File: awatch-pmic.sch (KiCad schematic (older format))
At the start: 16 parts, among them J301 Conn_01x02, U301 MAX14690

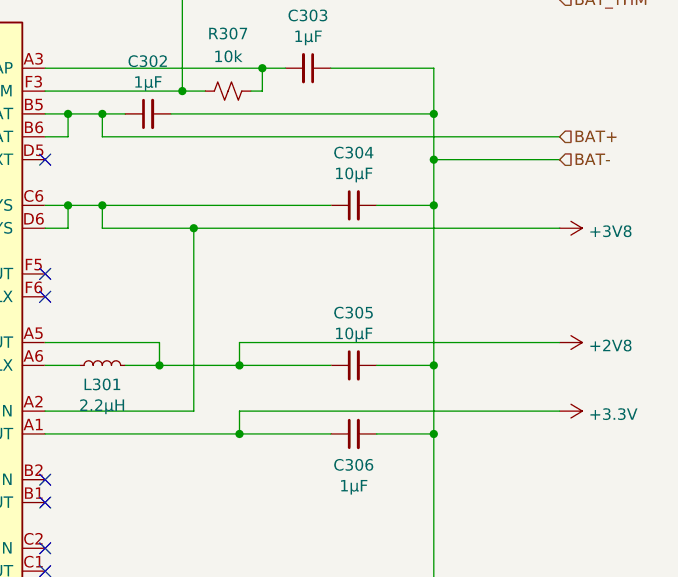
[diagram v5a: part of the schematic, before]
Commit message: Add footprints.
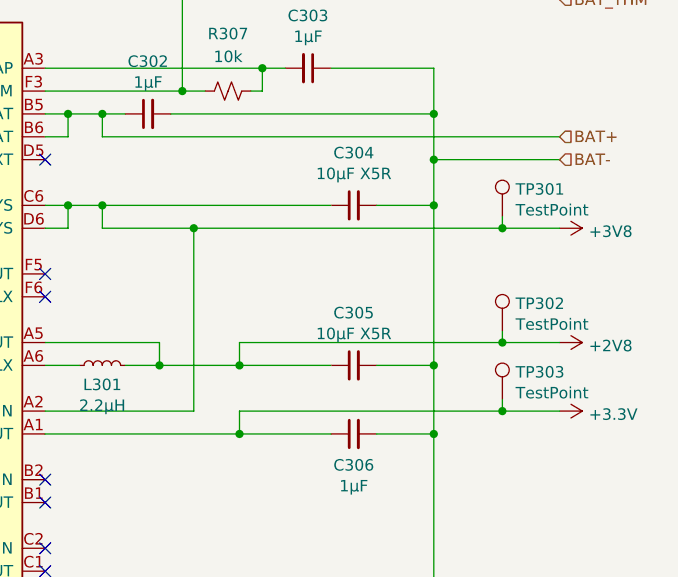
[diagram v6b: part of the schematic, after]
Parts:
- added TP301, TP302, TP303: TestPoint, TestPoint:TestPoint_Pad_D1.5mm, symbol Connector:TestPoint
- C301, C302, C303, C306: footprint (none) -> Capacitor_SMD:C_0603_1608Metric
- C304, C305: value 10µF -> 10µF X5R; footprint (none) -> Capacitor_SMD:C_0603_1608Metric
- J301: footprint (none) -> Connector_PinSocket_2.54mm:PinSocket_1x02_P2.54mm_Vertical
- L301: footprint (none) -> Inductor_SMD:L_0603_1608Metric
- R301, R302, R303, R304, R305, R306, R307: footprint (none) -> Resistor_SMD:R_0603_1608Metric
- U301: footprint (none) -> awatch2-footprints:WLP-36_2.69x2.44mm_Layout6x6_P0.4mm_Ball0.22mm_Pad0.2mm_NSMD
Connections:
- net +2V8: now also TP302.1
- net +3V3: now also TP303.1
- net +3V8: now also TP301.1
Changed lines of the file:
@@
 EESchema Schematic File Version 4
+LIBS:awatch2-cache
 EELAYER 26 0
 EELAYER END
@@
 F 0 "R302" H 3532 3554 50  0000 R CNN
 F 1 "10k" H 3532 3645 50  0000 R CNN
-F 2 "" H 3600 3600 50  0001 C CNN
+F 2 "Resistor_SMD:R_0603_1608Metric" H 3600 3600 50  0001 C CNN
 F 3 "~" H 3600 3600 50  0001 C CNN
 	1    3600 3600
@@
 F 0 "C301" H 3542 2096 50  0000 L CNN
 F 1 "1µF" H 3542 2005 50  0000 L CNN
-F 2 "" H 3450 2050 50  0001 C CNN
+F 2 "Capacitor_SMD:C_0603_1608Metric" H 3450 2050 50  0001 C CNN
 F 3 "~" H 3450 2050 50  0001 C CNN
 	1    3450 2050
@@
 F 0 "R304" V 3795 2200 50  0000 C CNN
 F 1 "12.5k" V 3886 2200 50  0000 C CNN
-F 2 "" H 4000 2200 50  0001 C CNN
+F 2 "Resistor_SMD:R_0603_1608Metric" H 4000 2200 50  0001 C CNN
 F 3 "~" H 4000 2200 50  0001 C CNN
 	1    4000 2200
@@
 F 0 "C303" V 6771 2200 50  0000 C CNN
 F 1 "1µF" V 6862 2200 50  0000 C CNN
-F 2 "" H 7000 2200 50  0001 C CNN
+F 2 "Capacitor_SMD:C_0603_1608Metric" H 7000 2200 50  0001 C CNN
 F 3 "~" H 7000 2200 50  0001 C CNN
 	1    7000 2200
@@
 F 0 "R307" V 6400 2300 50  0000 C CNN
 F 1 "10k" V 6500 2300 50  0000 C CNN
-F 2 "" H 6650 2300 50  0001 C CNN
+F 2 "Resistor_SMD:R_0603_1608Metric" H 6650 2300 50  0001 C CNN
 F 3 "~" H 6650 2300 50  0001 C CNN
 	1    6650 2300
@@
 F 0 "C302" V 6529 2400 50  0000 C CNN
 F 1 "1µF" V 6438 2400 50  0000 C CNN
-F 2 "" H 6300 2400 50  0001 C CNN
+F 2 "Capacitor_SMD:C_0603_1608Metric" H 6300 2400 50  0001 C CNN
 F 3 "~" H 6300 2400 50  0001 C CNN
 	1    6300 2400
@@
 P 7200 2800
 F 0 "C304" V 7429 2800 50  0000 C CNN
-F 1 "10µF" V 7338 2800 50  0000 C CNN
-F 2 "" H 7200 2800 50  0001 C CNN
+F 1 "10µF X5R" V 7338 2800 50  0000 C CNN
+F 2 "Capacitor_SMD:C_0603_1608Metric" H 7200 2800 50  0001 C CNN
 F 3 "~" H 7200 2800 50  0001 C CNN
 	1    7200 2800
@@
 F 0 "L301" V 6015 3500 50  0000 C CNN
 F 1 "2.2µH" V 5924 3500 50  0000 C CNN
-F 2 "" H 6100 3500 50  0001 C CNN
+F 2 "Inductor_SMD:L_0603_1608Metric" H 6100 3500 50  0001 C CNN
 F 3 "~" H 6100 3500 50  0001 C CNN
 	1    6100 3500
@@
 P 7200 3500
 F 0 "C305" V 7429 3500 50  0000 C CNN
-F 1 "10µF" V 7338 3500 50  0000 C CNN
-F 2 "" H 7200 3500 50  0001 C CNN
+F 1 "10µF X5R" V 7338 3500 50  0000 C CNN
+F 2 "Capacitor_SMD:C_0603_1608Metric" H 7200 3500 50  0001 C CNN
 F 3 "~" H 7200 3500 50  0001 C CNN
 	1    7200 3500
@@
 	6700 3500 6700 3400
 Wire Wire Line
-	6700 3400 8100 3400
+	6700 3400 7850 3400
 Connection ~ 6700 3500
 Wire Wire Line
@@
 F 0 "U301" H 5225 2166 50  0000 C CNN
 F 1 "MAX14690" H 5225 2075 50  0000 C CNN
-F 2 "" H 4700 2000 50  0001 C CNN
+F 2 "awatch2-footprints:WLP-36_2.69x2.44mm_Layout6x6_P0.4mm_Ball0.22mm_Pad0.2mm_NSMD" H 4700 2000 50  0001 C CNN
 F 3 "" H 4700 2000 50  0001 C CNN
 	1    4700 2000
@@
 F 0 "R306" V 3895 3800 50  0000 C CNN
 F 1 "0" V 3986 3800 50  0000 C CNN
-F 2 "" H 4100 3800 50  0001 C CNN
+F 2 "Resistor_SMD:R_0603_1608Metric" H 4100 3800 50  0001 C CNN
 F 3 "~" H 4100 3800 50  0001 C CNN
 	1    4100 3800
@@
 F 0 "R301" V 3650 2700 50  0000 C CNN
 F 1 "0" V 3750 2700 50  0000 C CNN
-F 2 "" H 3500 2700 50  0001 C CNN
+F 2 "Resistor_SMD:R_0603_1608Metric" H 3500 2700 50  0001 C CNN
 F 3 "~" H 3500 2700 50  0001 C CNN
 	1    3500 2700
@@
 F 0 "R303" V 3500 2800 50  0000 C CNN
 F 1 "0" V 3600 2800 50  0000 C CNN
-F 2 "" H 3750 2800 50  0001 C CNN
+F 2 "Resistor_SMD:R_0603_1608Metric" H 3750 2800 50  0001 C CNN
 F 3 "~" H 3750 2800 50  0001 C CNN
 	1    3750 2800
@@
 F 0 "R305" V 4113 3000 50  0000 C CNN
 F 1 "0" V 4204 3000 50  0000 C CNN
-F 2 "" H 4000 3000 50  0001 C CNN
+F 2 "Resistor_SMD:R_0603_1608Metric" H 4000 3000 50  0001 C CNN
 F 3 "~" H 4000 3000 50  0001 C CNN
 	1    4000 3000
@@
 F 0 "C306" V 7063 3800 50  0000 C CNN
 F 1 "1µF" V 6972 3800 50  0000 C CNN
-F 2 "" H 7200 3800 50  0001 C CNN
+F 2 "Capacitor_SMD:C_0603_1608Metric" H 7200 3800 50  0001 C CNN
 F 3 "~" H 7200 3800 50  0001 C CNN
 	1    7200 3800
@@
 	6700 3800 6700 3700
 Wire Wire Line
-	6700 3700 8100 3700
+	6700 3700 7850 3700
 Connection ~ 6700 3800
 Wire Wire Line
@@
 Connection ~ 6500 2900
 Wire Wire Line
-	6500 2900 8100 2900
+	6500 2900 7850 2900
 $Comp
 L power:+3.3V #PWR0134
@@
 F 0 "J301" H 3830 1542 50  0000 L CNN
 F 1 "Conn_01x02" H 3830 1451 50  0000 L CNN
-F 2 "" H 3750 1550 50  0001 C CNN
+F 2 "Connector_PinSocket_2.54mm:PinSocket_1x02_P2.54mm_Vertical" H 3750 1550 50  0001 C CNN
 F 3 "~" H 3750 1550 50  0001 C CNN
 	1    3750 1550
@@
 Wire Wire Line
 	6450 2300 6550 2300
+$Comp
+L Connector:TestPoint TP301
+U 1 1 5C869613
+P 7850 2850
+F 0 "TP301" H 7908 2970 50  0000 L CNN
+F 1 "TestPoint" H 7908 2879 50  0000 L CNN
+F 2 "TestPoint:TestPoint_Pad_D1.5mm" H 8050 2850 50  0001 C CNN
+F 3 "~" H 8050 2850 50  0001 C CNN
+	1    7850 2850
+	1    0    0    -1
+$EndComp
+Wire Wire Line
+	7850 2850 7850 2900
+Connection ~ 7850 2900
+Wire Wire Line
+	7850 2900 8100 2900
+$Comp
+L Connector:TestPoint TP302
+U 1 1 5C86C287
+P 7850 3350
+F 0 "TP302" H 7908 3470 50  0000 L CNN
+F 1 "TestPoint" H 7908 3379 50  0000 L CNN
+F 2 "TestPoint:TestPoint_Pad_D1.5mm" H 8050 3350 50  0001 C CNN
+F 3 "~" H 8050 3350 50  0001 C CNN
+	1    7850 3350
+	1    0    0    -1
+$EndComp
+Wire Wire Line
+	7850 3350 7850 3400
+Connection ~ 7850 3400
+Wire Wire Line
+	7850 3400 8100 3400
+$Comp
+L Connector:TestPoint TP303
+U 1 1 5C86F002
+P 7850 3650
+F 0 "TP303" H 7908 3770 50  0000 L CNN
+F 1 "TestPoint" H 7908 3679 50  0000 L CNN
+F 2 "TestPoint:TestPoint_Pad_D1.5mm" H 8050 3650 50  0001 C CNN
+F 3 "~" H 8050 3650 50  0001 C CNN
+	1    7850 3650
+	1    0    0    -1
+$EndComp
+Wire Wire Line
+	7850 3650 7850 3700
+Connection ~ 7850 3700
+Wire Wire Line
+	7850 3700 8100 3700
 $EndSCHEMATC

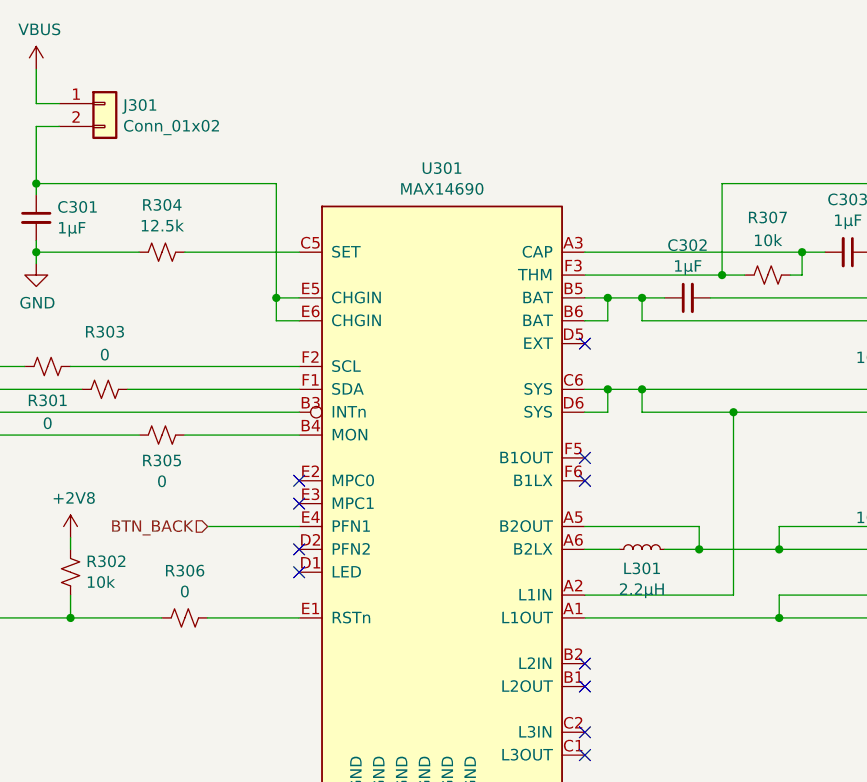
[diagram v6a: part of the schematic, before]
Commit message: PMIC relative placement and routing
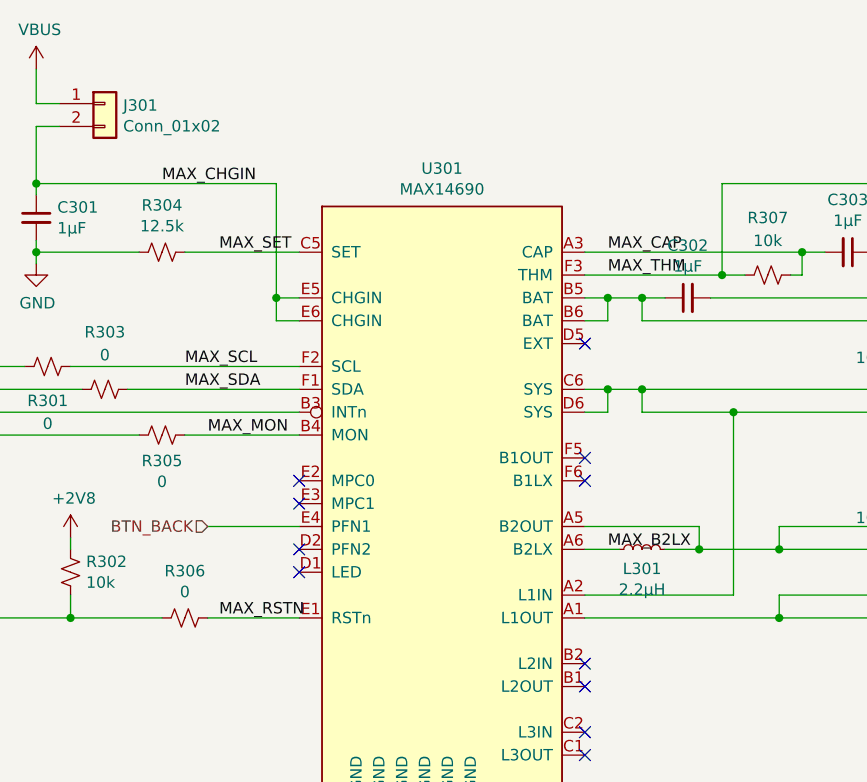
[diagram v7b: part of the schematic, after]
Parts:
- J301: footprint Connector_PinSocket_2.54mm:PinSocket_1x02_P2.54mm_Vertical -> Connector_PinHeader_2.54mm:PinHeader_1x02_P2.54mm_Vertical
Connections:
- net MAX_CAP: now reaches C303.2, R307.1, U301.A3 (CAP)
- net MAX_B2LX: now reaches L301.1, U301.A6 (B2LX)
- net MAX_MON: now reaches R305.1, U301.B4 (MON)
- net MAX_SET: now reaches R304.1, U301.C5 (SET)
- net MAX_RSTN: now reaches R306.1, U301.E1 (RSTn)
- net MAX_CHGIN: now reaches C301.1, J301.2 (Pin_2), U301.E5 (CHGIN), U301.E6 (CHGIN)
- net MAX_SDA: now reaches R303.1, U301.F1 (SDA)
- net MAX_SCL: now reaches R301.1, U301.F2 (SCL)
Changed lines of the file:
@@
 F 0 "J301" H 3830 1542 50  0000 L CNN
 F 1 "Conn_01x02" H 3830 1451 50  0000 L CNN
-F 2 "Connector_PinSocket_2.54mm:PinSocket_1x02_P2.54mm_Vertical" H 3750 1550 50  0001 C CNN
+F 2 "Connector_PinHeader_2.54mm:PinHeader_1x02_P2.54mm_Vertical" H 3750 1550 50  0001 C CNN
 F 3 "~" H 3750 1550 50  0001 C CNN
 	1    3750 1550
@@
 Wire Wire Line
 	7850 3700 8100 3700
+Text Label 4250 2200 0    50   ~ 0
+MAX_SET
+Text Label 4000 1900 0    50   ~ 0
+MAX_CHGIN
+Text Label 4100 2700 0    50   ~ 0
+MAX_SCL
+Text Label 4100 2800 0    50   ~ 0
+MAX_SDA
+Text Label 4200 3000 0    50   ~ 0
+MAX_MON
+Text Label 4250 3800 0    50   ~ 0
+MAX_RSTN
+Text Label 5950 2200 0    50   ~ 0
+MAX_CAP
+Text Label 5950 2300 0    50   ~ 0
+MAX_THM
+Text Label 5950 3500 0    50   ~ 0
+MAX_B2LX
 $EndSCHEMATC

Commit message: approx. final layout
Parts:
- C301, C302, C303, C306: value 1µF -> 1.0µF X7R; DigiKey PN (none) -> 1276-1946-1-ND
- C304, C305: DigiKey PN (none) -> 490-12538-1-ND
- U301: value MAX14690 -> MAX14690A; DigiKey PN (none) -> MOUSER: 700-MAX14690AEWX+
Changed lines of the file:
@@
 $Descr A4 11693 8268
 encoding utf-8
-Sheet 3 9
+Sheet 3 10
 Title "AWatch2"
 Date ""
@@
 P 3450 2050
 F 0 "C301" H 3542 2096 50  0000 L CNN
-F 1 "1µF" H 3542 2005 50  0000 L CNN
+F 1 "1.0µF X7R" H 3542 2005 50  0000 L CNN
 F 2 "Capacitor_SMD:C_0603_1608Metric" H 3450 2050 50  0001 C CNN
 F 3 "~" H 3450 2050 50  0001 C CNN
+F 4 "1276-1946-1-ND" H 0   0   50  0001 C CNN "DigiKey PN"
 	1    3450 2050
 	1    0    0    -1
@@
 P 7000 2200
 F 0 "C303" V 6771 2200 50  0000 C CNN
-F 1 "1µF" V 6862 2200 50  0000 C CNN
+F 1 "1.0µF X7R" V 6862 2200 50  0000 C CNN
 F 2 "Capacitor_SMD:C_0603_1608Metric" H 7000 2200 50  0001 C CNN
 F 3 "~" H 7000 2200 50  0001 C CNN
+F 4 "1276-1946-1-ND" H 0   0   50  0001 C CNN "DigiKey PN"
 	1    7000 2200
 	0    1    1    0
@@
 P 6300 2400
 F 0 "C302" V 6529 2400 50  0000 C CNN
-F 1 "1µF" V 6438 2400 50  0000 C CNN
+F 1 "1.0µF X7R" V 6438 2400 50  0000 C CNN
 F 2 "Capacitor_SMD:C_0603_1608Metric" H 6300 2400 50  0001 C CNN
 F 3 "~" H 6300 2400 50  0001 C CNN
+F 4 "1276-1946-1-ND" H 0   0   50  0001 C CNN "DigiKey PN"
 	1    6300 2400
 	0    -1   -1   0
@@
 F 2 "Capacitor_SMD:C_0603_1608Metric" H 7200 2800 50  0001 C CNN
 F 3 "~" H 7200 2800 50  0001 C CNN
+F 4 "490-12538-1-ND" H 0   0   50  0001 C CNN "DigiKey PN"
 	1    7200 2800
 	0    -1   -1   0
@@
 F 2 "Capacitor_SMD:C_0603_1608Metric" H 7200 3500 50  0001 C CNN
 F 3 "~" H 7200 3500 50  0001 C CNN
+F 4 "490-12538-1-ND" H 0   0   50  0001 C CNN "DigiKey PN"
 	1    7200 3500
 	0    -1   -1   0
@@
 P 4700 2000
 F 0 "U301" H 5225 2166 50  0000 C CNN
-F 1 "MAX14690" H 5225 2075 50  0000 C CNN
+F 1 "MAX14690A" H 5225 2075 50  0000 C CNN
 F 2 "awatch2-footprints:WLP-36_2.69x2.44mm_Layout6x6_P0.4mm_Ball0.22mm_Pad0.2mm_NSMD" H 4700 2000 50  0001 C CNN
 F 3 "" H 4700 2000 50  0001 C CNN
+F 4 "MOUSER: 700-MAX14690AEWX+" H 0   0   50  0001 C CNN "DigiKey PN"
 	1    4700 2000
 	1    0    0    -1
@@
 P 7200 3800
 F 0 "C306" V 7063 3800 50  0000 C CNN
-F 1 "1µF" V 6972 3800 50  0000 C CNN
+F 1 "1.0µF X7R" V 6972 3800 50  0000 C CNN
 F 2 "Capacitor_SMD:C_0603_1608Metric" H 7200 3800 50  0001 C CNN
 F 3 "~" H 7200 3800 50  0001 C CNN
+F 4 "1276-1946-1-ND" H 0   0   50  0001 C CNN "DigiKey PN"
 	1    7200 3800
 	0    -1   -1   0
